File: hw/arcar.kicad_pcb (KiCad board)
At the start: 2 copper layers, 60 x 36 mm, 53 parts, among them J1 USB_B_Micro, J2 MOTOR, J3 POWER, M1 screw, M2 screw, P1 AVR_ISP_02X03, SW1 SW_Push, U1 USBLC6-2SC6, U2 ATMEGA328PB-AU, U3 CP2102, U4 ULN2003A, U5 LSM9DS1, U6 TLE52062GAUMA1, U7 RN4871, U8 MCP1804T-3302I/DB

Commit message: board updated
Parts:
- moved U4 0.52 mm to (63.6, 147.8)
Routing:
- net /MISO: track 106.5 -> 95.2 mm
- net GND: track 44.2 -> 47.4 mm, vias 17 -> 20
- net Net-(R6-Pad2): track 7.97 -> 8.87 mm
- net /~RST: track 126.1 -> 125.2 mm
- net Net-(R7-Pad2): track 7.27 -> 7.95 mm

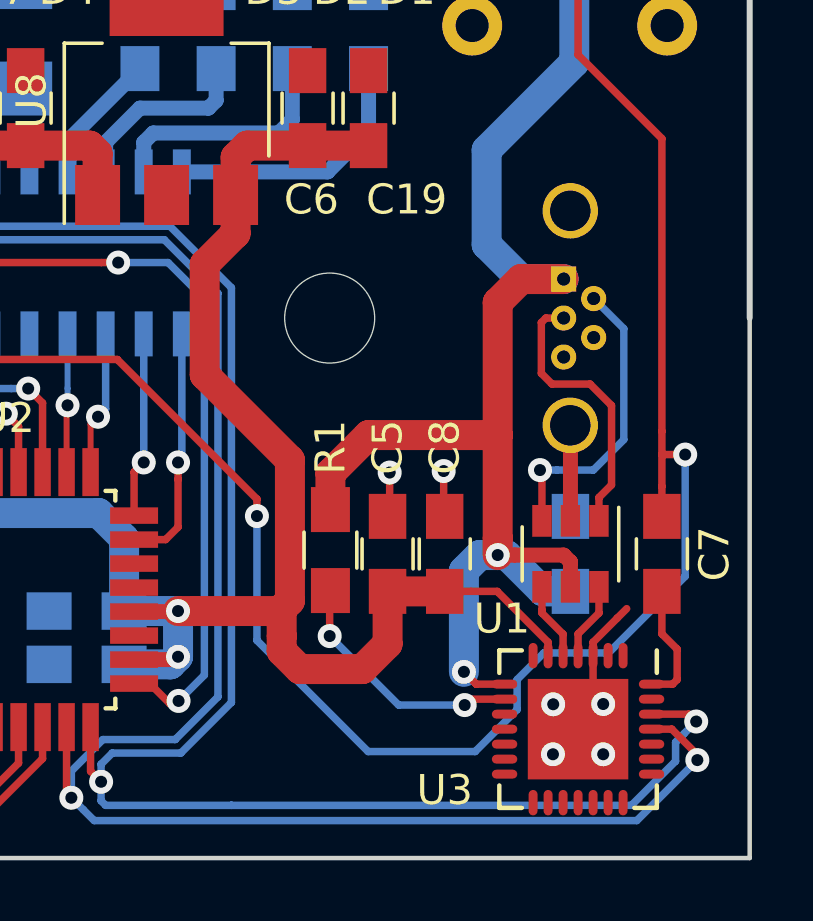
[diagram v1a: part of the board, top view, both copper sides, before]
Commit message: added wykys logo
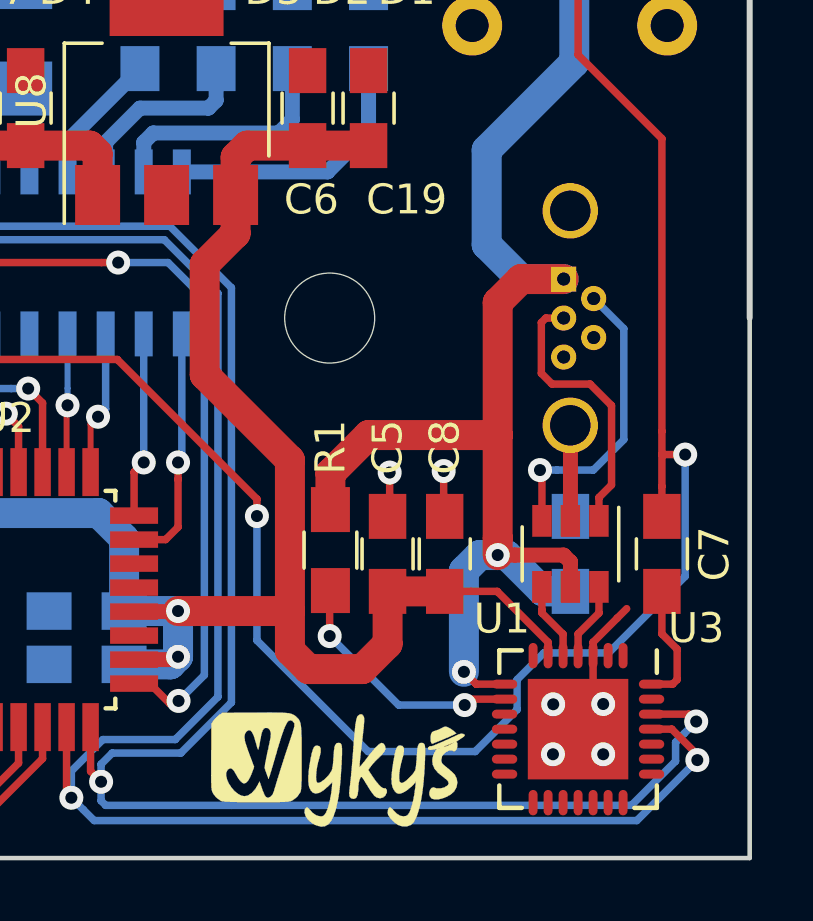
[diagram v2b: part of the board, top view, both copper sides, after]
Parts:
- added G***: LOGO, wyk_logo:wykys_small_skill, F.Cu at (73.3, 165.0)

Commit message: board updated
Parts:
- added G***: LOGO, wyk_logo:VUT-FEKT_small, F.Cu at (84.8, 147.6)
- moved G*** 0.20 mm to (73.1, 165.1)
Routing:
- net +3V3: track 151.5 -> 149.1 mm
- net GND: vias 20 -> 36
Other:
- board text added: "ARCAR V1 2017"
- board text added: "GND"
- board text added: "MISO"
- board text added: "MOSI"
- board text added: "SCK"
- board text added: "VCC"
- board text added: "~RST"

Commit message: board updated
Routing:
- net GND: vias 36 -> 35
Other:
- board text added: "M"
- board text added: "POWER"
- board text added: "RESET"
- board text added: "x"
- board text added: "y"
- board text added: "z"
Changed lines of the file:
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@@
   (general
     (thickness 1.6)
-    (drawings 40)
-    (tracks 669)
+    (drawings 59)
+    (tracks 668)
     (zones 0)
     (modules 55)
@@
     (tags "CMS SOT")
     (attr smd)
-    (fp_text reference U8 (at 0 -4.5 90) (layer F.SilkS)
+    (fp_text reference U8 (at -4.191 -4.6355 180) (layer F.SilkS)
       (effects (font (size 1 1) (thickness 0.15)))
     )
@@
     (descr "CP, Radial series, Radial, pin pitch=1.50mm, , diameter=4mm, Electrolytic Capacitor")
     (tags "CP Radial series Radial pin pitch 1.50mm  diameter 4mm Electrolytic Capacitor")
-    (fp_text reference C17 (at -0.127 3.429) (layer F.SilkS)
+    (fp_text reference C17 (at -1.778 -2.159) (layer F.SilkS)
       (effects (font (size 1 1) (thickness 0.15)))
     )
@@
     (tags "capacitor 0805")
     (attr smd)
-    (fp_text reference C5 (at 3.556 0 90) (layer F.SilkS)
+    (fp_text reference C5 (at 4.1275 0 90) (layer F.SilkS)
       (effects (font (size 1 1) (thickness 0.15)))
     )
@@
     (tags "capacitor 0805")
     (attr smd)
-    (fp_text reference C6 (at -3.048 0.127 180) (layer F.SilkS)
+    (fp_text reference C6 (at -3.1115 0 270) (layer F.SilkS)
       (effects (font (size 1 1) (thickness 0.15)))
     )
@@
     (tags "capacitor 0805")
     (attr smd)
-    (fp_text reference C8 (at 3.556 0 90) (layer F.SilkS)
+    (fp_text reference C8 (at 4.1275 0 90) (layer F.SilkS)
       (effects (font (size 1 1) (thickness 0.15)))
     )
@@
     (tags "capacitor 0805")
     (attr smd)
-    (fp_text reference C9 (at 4.826 -1.611 90) (layer F.SilkS)
+    (fp_text reference C9 (at 3.7465 0.04 90) (layer F.SilkS)
       (effects (font (size 1 1) (thickness 0.15)))
     )
@@
     (tags "capacitor 0805")
     (attr smd)
-    (fp_text reference C10 (at 4.826 0.294 90) (layer F.SilkS)
+    (fp_text reference C10 (at 4.191 -0.0235 90) (layer F.SilkS)
       (effects (font (size 1 1) (thickness 0.15)))
     )
@@
     (tags "capacitor 0805")
     (attr smd)
-    (fp_text reference C11 (at -4.826 -2.199 270) (layer F.SilkS)
+    (fp_text reference C11 (at -4.1275 -0.04 270) (layer F.SilkS)
       (effects (font (size 1 1) (thickness 0.15)))
     )
@@
     (descr "CP, Radial series, Radial, pin pitch=1.50mm, , diameter=4mm, Electrolytic Capacitor")
     (tags "CP Radial series Radial pin pitch 1.50mm  diameter 4mm Electrolytic Capacitor")
-    (fp_text reference C15 (at -2.3495 2.3495) (layer F.SilkS)
+    (fp_text reference C15 (at -2.032 -2.159) (layer F.SilkS)
       (effects (font (size 1 1) (thickness 0.15)))
     )
@@
     (tags "Diode SMA (DO-214AC)")
     (attr smd)
-    (fp_text reference D6 (at -4.62 0.525) (layer B.SilkS)
+    (fp_text reference D6 (at -4.874 1.033) (layer B.SilkS)
       (effects (font (size 1 1) (thickness 0.15)) (justify mirror))
     )
@@
     (tags "Diode SMA (DO-214AC)")
     (attr smd)
-    (fp_text reference D8 (at -4.62 0.265) (layer B.SilkS)
+    (fp_text reference D8 (at -4.874 1.281) (layer B.SilkS)
       (effects (font (size 1 1) (thickness 0.15)) (justify mirror))
     )
@@
     (descr "Through hole straight pin header, 1x02, 2.54mm pitch, single row")
     (tags "Through hole pin header THT 1x02 2.54mm single row")
-    (fp_text reference J2 (at 2.54 1.27 180) (layer F.SilkS)
+    (fp_text reference J2 (at 0 4.953 180) (layer F.SilkS)
       (effects (font (size 1 1) (thickness 0.15)))
     )
@@
     (tags "resistor 0805")
     (attr smd)
-    (fp_text reference R1 (at -3.429 0 270) (layer F.SilkS)
+    (fp_text reference R1 (at -3.81 0 270) (layer F.SilkS)
       (effects (font (size 1 1) (thickness 0.15)))
     )
@@
       (effects (font (size 1 1) (thickness 0.15)))
     )
-    (fp_text user %R (at 0 -2.7) (layer F.Fab)
+    (fp_text user %R (at -0.129 0.114) (layer F.Fab)
       (effects (font (size 1 1) (thickness 0.15)))
     )
@@
     (tags "capacitor 0805")
     (attr smd)
-    (fp_text reference C19 (at -3.048 1.27 180) (layer F.SilkS)
+    (fp_text reference C19 (at 0.0635 1.9685 270) (layer F.SilkS)
       (effects (font (size 1 1) (thickness 0.15)))
     )
@@
       (rotate (xyz 0 0 0))
     )
+  )
+  (gr_text z (at 51 155) (layer F.SilkS)
+    (effects (font (size 1 1) (thickness 0.25)))
+  )
+  (gr_text y (at 51 156.5) (layer F.SilkS)
+    (effects (font (size 1 1) (thickness 0.25)))
+  )
+  (gr_text x (at 53 155) (layer F.SilkS)
+    (effects (font (size 1 1) (thickness 0.25)))
+  )
+  (gr_poly (pts (xy 52 159) (xy 53 158) (xy 51 158)) (layer F.SilkS) (width 0.15))
+  (gr_poly (pts (xy 55 156) (xy 54 157) (xy 54 155)) (layer F.SilkS) (width 0.15))
+  (gr_line (start 52 156) (end 52 159) (layer F.SilkS) (width 0.15))
+  (gr_line (start 52 156) (end 55 156) (layer F.SilkS) (width 0.15))
+  (gr_text RESET (at 81.28 138.049) (layer F.SilkS)
+    (effects (font (size 1 1) (thickness 0.25)))
+  )
+  (gr_line (start 51.435 161.925) (end 52.07 161.925) (layer F.SilkS) (width 0.15))
+  (gr_line (start 47.625 161.925) (end 46.99 161.925) (layer F.SilkS) (width 0.15))
+  (gr_line (start 51.435 162.56) (end 50.8 162.56) (layer F.SilkS) (width 0.15))
+  (gr_line (start 51.435 161.29) (end 51.435 162.56) (layer F.SilkS) (width 0.15))
+  (gr_line (start 50.8 161.29) (end 51.435 161.29) (layer F.SilkS) (width 0.15))
+  (gr_line (start 47.625 162.56) (end 48.26 162.56) (layer F.SilkS) (width 0.15))
+  (gr_line (start 47.625 161.29) (end 47.625 162.56) (layer F.SilkS) (width 0.15))
+  (gr_line (start 48.26 161.29) (end 47.625 161.29) (layer F.SilkS) (width 0.15))
+  (gr_text M (at 49.53 161.925) (layer F.SilkS)
+    (effects (font (size 1 1) (thickness 0.25)))
+  )
+  (gr_circle (center 49.53 161.925) (end 50.8 161.925) (layer F.SilkS) (width 0.15))
+  (gr_text POWER (at 46.5455 136.525) (layer F.SilkS)
+    (effects (font (size 1 1) (thickness 0.25)))
   )
   (gr_text VCC (at 32.512 134.112) (layer F.SilkS)
@@
   (gr_line (start 53 149) (end 55 151) (layer Dwgs.User) (width 0.2))
   (gr_line (start 50 150) (end 54 150) (layer Dwgs.User) (width 0.2))
+  (via (at 64.77 137.16) (size 0.8) (drill 0.4) (layers F.Cu B.Cu) (net 1))
   (via (at 43.18 133.9215) (size 0.8) (drill 0.4) (layers F.Cu B.Cu) (net 1))
-  (via (at 64.516 136.398) (size 0.8) (drill 0.4) (layers F.Cu B.Cu) (net 1))
   (via (at 50.8635 147.6375) (size 0.8) (drill 0.4) (layers F.Cu B.Cu) (net 1))
   (via (at 55.372 162.8775) (size 0.8) (drill 0.4) (layers F.Cu B.Cu) (net 1))
   (via (at 76.0095 146.2405) (size 0.8) (drill 0.4) (layers F.Cu B.Cu) (net 1))
-  (via (at 70.739 164.338) (size 0.8) (drill 0.4) (layers F.Cu B.Cu) (net 1))
   (via (at 51.2445 146.1135) (size 0.8) (drill 0.4) (layers F.Cu B.Cu) (net 1))
   (via (at 39.9415 137.4775) (size 0.8) (drill 0.4) (layers F.Cu B.Cu) (net 1))
@@
   (via (at 35.052 143.9545) (size 0.8) (drill 0.4) (layers F.Cu B.Cu) (net 1))
   (via (at 35.433 153.6065) (size 0.8) (drill 0.4) (layers F.Cu B.Cu) (net 1))
-  (via (at 33.528 155.6385) (size 0.8) (drill 0.4) (layers F.Cu B.Cu) (net 1))
-  (via (at 32.385 155.702) (size 0.8) (drill 0.4) (layers F.Cu B.Cu) (net 1))
-  (via (at 31.115 155.702) (size 0.8) (drill 0.4) (layers F.Cu B.Cu) (net 1))
-  (via (at 29.9085 155.702) (size 0.8) (drill 0.4) (layers F.Cu B.Cu) (net 1))
-  (via (at 28.7655 155.702) (size 0.8) (drill 0.4) (layers F.Cu B.Cu) (net 1))
+  (via (at 33.528 155.321) (size 0.8) (drill 0.4) (layers F.Cu B.Cu) (net 1))
+  (via (at 32.385 155.321) (size 0.8) (drill 0.4) (layers F.Cu B.Cu) (net 1))
+  (via (at 31.115 155.321) (size 0.8) (drill 0.4) (layers F.Cu B.Cu) (net 1))
+  (via (at 29.972 155.321) (size 0.8) (drill 0.4) (layers F.Cu B.Cu) (net 1))
+  (via (at 28.829 155.321) (size 0.8) (drill 0.4) (layers F.Cu B.Cu) (net 1))
   (via (at 33.4645 164.084) (size 0.8) (drill 0.4) (layers F.Cu B.Cu) (net 1))
   (via (at 35.8775 161.29) (size 0.8) (drill 0.4) (layers F.Cu B.Cu) (net 1))
